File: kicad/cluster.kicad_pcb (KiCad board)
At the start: 2 copper layers, 24.5 x 36.5 mm, 16 parts, among them J1 Conn_01x07

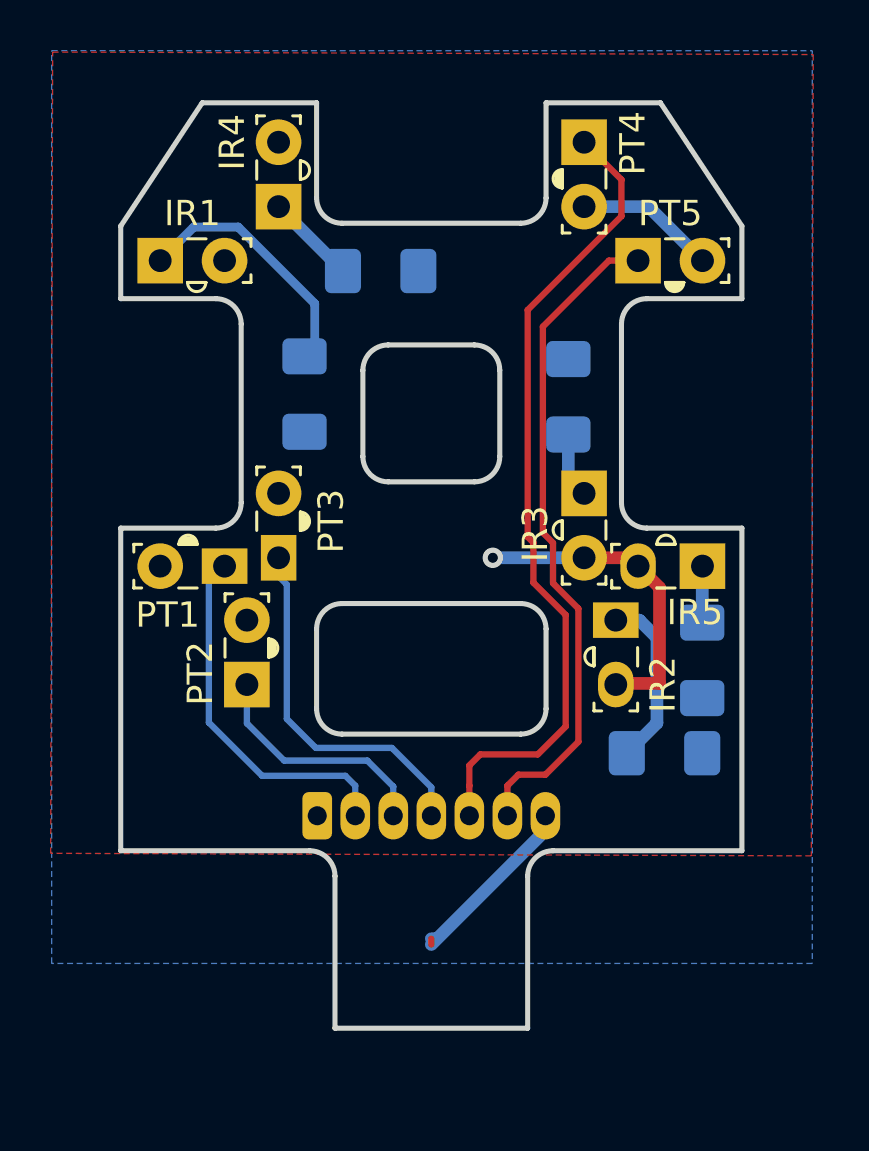
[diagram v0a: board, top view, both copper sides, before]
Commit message: Edit cluster board for choc key switch
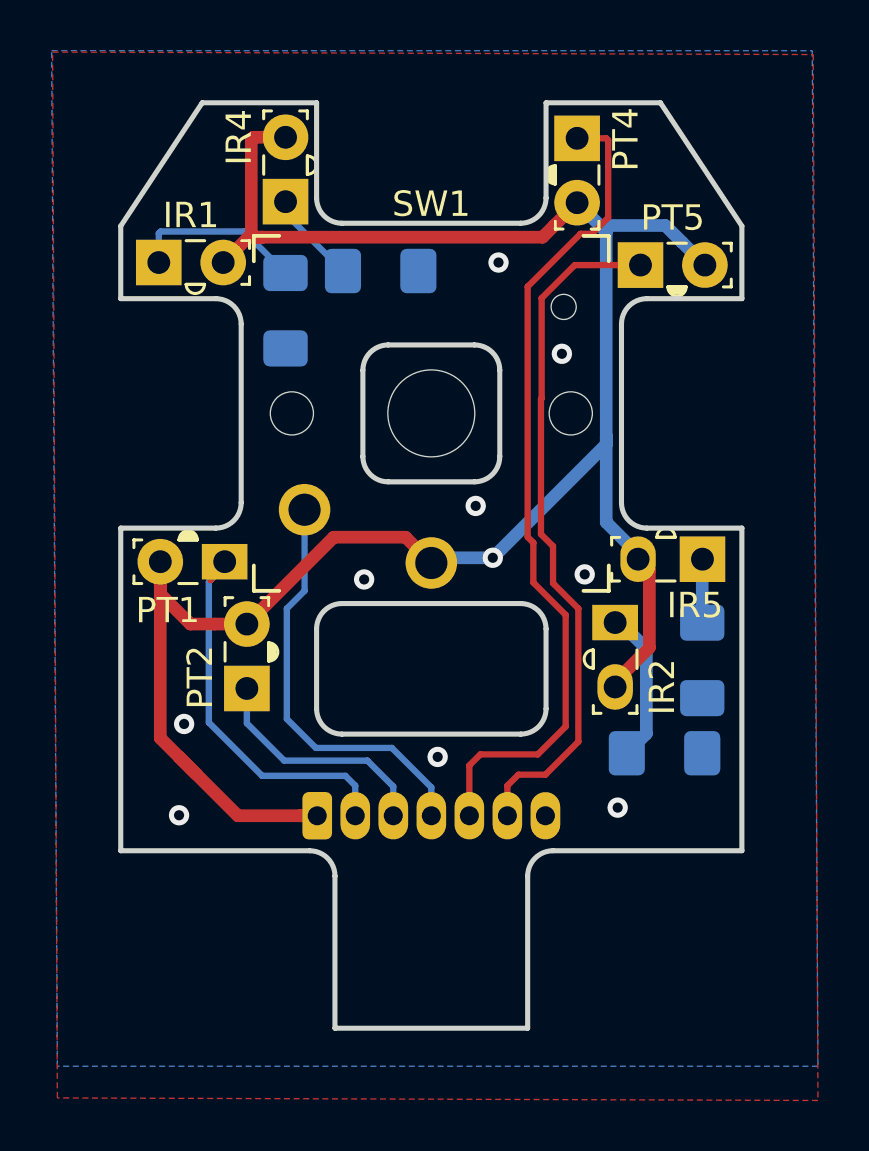
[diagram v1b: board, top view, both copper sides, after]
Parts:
- removed IR3: IR908-7C-F, lalboard:IR908-7C-F
- removed PT3: PT908-7B-F, lalboard:PT908-7C-F
- removed R3: 270, Resistor_SMD:R_1206_3216Metric_Pad1.42x1.75mm_HandSolder
- added SW1: SW_Push, lalboard:SW_CHOC, F.Cu at (162.4, 75.5)
- IR1, IR2, IR4, IR5: value IR908-7C-F -> OP140C
- PT1, PT2, PT4, PT5: value PT908-7B-F -> OP550A
- R1, R2, R4, R5: value 270 -> 150
- moved R1 3.37 mm to (156.7, 71.5)
- moved IR4 0.34 mm to (156.7, 67.2)
- moved PT4 0.32 mm to (168.2, 64.7)
- moved IR5 0.28 mm to (173.1, 81.3)
- moved PT5 0.20 mm to (170.7, 69.7)
- moved PT1 0.18 mm to (154.3, 81.4)
- moved PT2 0.16 mm to (155.2, 86.4)
- moved IR2 0.10 mm to (169.7, 83.8)
- moved IR1 0.09 mm to (151.7, 69.6)
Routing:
- net +5V: track 18.4 -> 86.6 mm
- net GND: track 7.76 -> 1.03 mm, vias 0 -> 9
- net Net-(IR1-Pad1): track 9.97 -> 6.86 mm
- net Net-(IR3-Pad1): track 2.58 -> 0.00 mm
- net C3: track 14.4 -> 16.5 mm
- net Net-(IR2-Pad1): track 6.96 -> 6.10 mm
- net C5: track 26.5 -> 27.3 mm
- net C4: track 32.2 -> 33.0 mm
- added copper zone on F.Cu, net GND
- removed copper zone on F.Cu, net +5V

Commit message: Customize
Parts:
- added R3: 5.1k, Resistor_SMD:R_0805_2012Metric_Pad1.15x1.40mm_HandSolder, B.Cu at (166.6, 80.6)
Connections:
- SW1 pad 1: +5V -> C3
- SW1 pad 2: C3 -> GND
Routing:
- net +5V: track 86.6 -> 91.3 mm, vias 1 -> 0
- net C3: track 16.5 -> 17.7 mm
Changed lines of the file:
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@@
   (general
     (thickness 1.6)
-    (drawings 172)
-    (tracks 118)
+    (drawings 174)
+    (tracks 119)
     (zones 0)
-    (modules 14)
+    (modules 15)
     (nets 12)
   )
@@
     (pad "" np_thru_hole circle (at 0 0) (size 3.429 3.429) (drill 3.429) (layers *.Cu *.Mask))
     (pad 2 thru_hole circle (at -5 3.8) (size 2.032 2.032) (drill 1.27) (layers *.Cu *.Mask)
+      (net 11 GND))
+    (pad 1 thru_hole circle (at 0 5.9) (size 2.032 2.032) (drill 1.27) (layers *.Cu *.Mask)
       (net 9 C3))
-    (pad 1 thru_hole circle (at 0 5.9) (size 2.032 2.032) (drill 1.27) (layers *.Cu *.Mask)
-      (net 1 +5V))
     (pad "" np_thru_hole circle (at 5.22 -4.2) (size 0.9906 0.9906) (drill 0.9906) (layers *.Cu *.Mask))
     (pad "" np_thru_hole circle (at 5.5 0) (size 1.7018 1.7018) (drill 1.7018) (layers *.Cu *.Mask))
     (pad "" np_thru_hole circle (at -5.5 0) (size 1.7018 1.7018) (drill 1.7018) (layers *.Cu *.Mask))
+  )
+  (module Resistor_SMD:R_0805_2012Metric_Pad1.15x1.40mm_HandSolder (layer B.Cu)
+    (at 166.6 80.575 90)
+    (descr "Resistor SMD 0805 (2012 Metric), square (rectangular) end terminal, IPC_7351 nominal with elongated pad for handsoldering. (Body size source: https://docs.google.com/spreadsheets/d/1BsfQQcO9C6DZCsRaXUlFlo91Tg2WpOkGARC1WS5S8t0/edit?usp=sharing), generated with kicad-footprint-generator")
+    (tags "resistor handsolder")
+    (attr smd)
+    (fp_text reference R3 (at 0 1.65 90) (layer B.SilkS)
+      (effects (font (size 1 1) (thickness 0.15)) (justify mirror))
+    )
+    (fp_text value 5.1k (at 0 -1.65 90) (layer B.Fab)
+      (effects (font (size 1 1) (thickness 0.15)) (justify mirror))
+    )
+    (fp_text user %R (at 0 0 90) (layer B.Fab)
+      (effects (font (size 0.5 0.5) (thickness 0.08)) (justify mirror))
+    )
+    (fp_line (start 1.85 -0.95) (end -1.85 -0.95) (layer B.CrtYd) (width 0.05))
+    (fp_line (start 1.85 0.95) (end 1.85 -0.95) (layer B.CrtYd) (width 0.05))
+    (fp_line (start -1.85 0.95) (end 1.85 0.95) (layer B.CrtYd) (width 0.05))
+    (fp_line (start -1.85 -0.95) (end -1.85 0.95) (layer B.CrtYd) (width 0.05))
+    (fp_line (start -0.261252 -0.71) (end 0.261252 -0.71) (layer B.SilkS) (width 0.12))
+    (fp_line (start -0.261252 0.71) (end 0.261252 0.71) (layer B.SilkS) (width 0.12))
+    (fp_line (start 1 -0.6) (end -1 -0.6) (layer B.Fab) (width 0.1))
+    (fp_line (start 1 0.6) (end 1 -0.6) (layer B.Fab) (width 0.1))
+    (fp_line (start -1 0.6) (end 1 0.6) (layer B.Fab) (width 0.1))
+    (fp_line (start -1 -0.6) (end -1 0.6) (layer B.Fab) (width 0.1))
+    (pad 2 smd roundrect (at 1.025 0 90) (size 1.15 1.4) (layers B.Cu B.Paste B.Mask) (roundrect_rratio 0.217391)
+      (net 1 +5V))
+    (pad 1 smd roundrect (at -1.025 0 90) (size 1.15 1.4) (layers B.Cu B.Paste B.Mask) (roundrect_rratio 0.217391)
+      (net 9 C3))
+    (model ${KISYS3DMOD}/Resistor_SMD.3dshapes/R_0805_2012Metric.wrl
+      (at (xyz 0 0 0))
+      (scale (xyz 1 1 1))
+      (rotate (xyz 0 0 0))
+    )
   )
   (module Resistor_SMD:R_1206_3216Metric_Pad1.42x1.75mm_HandSolder (layer B.Cu)
@@
       (rotate (xyz 0 0 0))
     )
+  )
+  (dimension 36.5 (width 0.15) (layer F.SilkS)
+    (gr_text "36.500 mm" (at 143.2 81.55 270) (layer F.SilkS)
+      (effects (font (size 1 1) (thickness 0.15)))
+    )
+    (feature1 (pts (xy 154.8 99.8) (xy 143.913579 99.8)))
+    (feature2 (pts (xy 154.8 63.3) (xy 143.913579 63.3)))
+    (crossbar (pts (xy 144.5 63.3) (xy 144.5 99.8)))
+    (arrow1a (pts (xy 144.5 99.8) (xy 143.913579 98.673496)))
+    (arrow1b (pts (xy 144.5 99.8) (xy 145.086421 98.673496)))
+    (arrow2a (pts (xy 144.5 63.3) (xy 143.913579 64.426504)))
+    (arrow2b (pts (xy 144.5 63.3) (xy 145.086421 64.426504)))
+  )
+  (dimension 24.5 (width 0.15) (layer F.SilkS)
+    (gr_text "24.500 mm" (at 162.45 55.4) (layer F.SilkS)
+      (effects (font (size 1 1) (thickness 0.15)))
+    )
+    (feature1 (pts (xy 174.7 68.160134) (xy 174.7 56.113579)))
+    (feature2 (pts (xy 150.2 68.160134) (xy 150.2 56.113579)))
+    (crossbar (pts (xy 150.2 56.7) (xy 174.7 56.7)))
+    (arrow1a (pts (xy 174.7 56.7) (xy 173.573496 57.286421)))
+    (arrow1b (pts (xy 174.7 56.7) (xy 173.573496 56.113579)))
+    (arrow2a (pts (xy 150.2 56.7) (xy 151.326504 57.286421)))
+    (arrow2b (pts (xy 150.2 56.7) (xy 151.326504 56.113579)))
   )
   (gr_text "finger cluster\nv0.1" (at 161.8 80.3) (layer B.SilkS)
@@
   (segment (start 169.77 86.2) (end 169.725 86.245) (width 0.5) (layer F.Cu) (net 1))
   (segment (start 170.275 81.245) (end 170.605 81.575) (width 0.5) (layer F.Cu) (net 1))
-  (via (at 164.875008 81.245) (size 0.8) (drill 0.4) (layers F.Cu B.Cu) (net 1))
-  (segment (start 162.655 81.245) (end 162.45 81.45) (width 0.5) (layer B.Cu) (net 1))
-  (segment (start 164.875008 81.245) (end 162.655 81.245) (width 0.5) (layer B.Cu) (net 1))
   (segment (start 169.349999 68.389999) (end 169.099999 68.139999) (width 0.5) (layer B.Cu) (net 1))
-  (segment (start 164.875008 81.245) (end 169.349999 76.770009) (width 0.5) (layer B.Cu) (net 1))
   (segment (start 172.340001 68.800001) (end 173.24 69.7) (width 0.5) (layer B.Cu) (net 1))
   (segment (start 171.679999 68.139999) (end 172.340001 68.800001) (width 0.5) (layer B.Cu) (net 1))
   (segment (start 169.099999 68.139999) (end 171.679999 68.139999) (width 0.5) (layer B.Cu) (net 1))
   (segment (start 168.2 67.24) (end 169.099999 68.139999) (width 0.5) (layer B.Cu) (net 1))
-  (segment (start 164.930008 81.3) (end 164.875008 81.245) (width 0.5) (layer B.Cu) (net 1))
   (segment (start 157.265 91.42) (end 157.95 91.42) (width 0.5) (layer F.Cu) (net 1))
   (segment (start 167.300001 68.139999) (end 168.2 67.24) (width 0.5) (layer F.Cu) (net 1))
@@
   (segment (start 151.76 82.672792) (end 152.947208 83.86) (width 0.5) (layer F.Cu) (net 1))
   (segment (start 151.76 81.4) (end 151.76 82.672792) (width 0.5) (layer F.Cu) (net 1))
-  (segment (start 161.434001 80.434001) (end 162.45 81.45) (width 0.5) (layer F.Cu) (net 1))
-  (segment (start 158.600999 80.434001) (end 161.434001 80.434001) (width 0.5) (layer F.Cu) (net 1))
-  (segment (start 155.175 83.86) (end 158.600999 80.434001) (width 0.5) (layer F.Cu) (net 1))
   (segment (start 170.605 81.1) (end 170.605 81.3) (width 0.5) (layer B.Cu) (net 1))
   (segment (start 169.349999 76.450001) (end 169.349999 79.844999) (width 0.5) (layer B.Cu) (net 1))
@@
   (segment (start 169.349999 76.450001) (end 169.349999 68.389999) (width 0.5) (layer B.Cu) (net 1))
   (segment (start 169.349999 76.770009) (end 169.349999 76.450001) (width 0.5) (layer B.Cu) (net 1))
+  (segment (start 168.855 79.55) (end 166.6 79.55) (width 0.5) (layer B.Cu) (net 1))
+  (segment (start 170.605 81.3) (end 168.855 79.55) (width 0.5) (layer B.Cu) (net 1))
+  (segment (start 155.139999 70.499999) (end 154.24 69.6) (width 0.5) (layer F.Cu) (net 1))
+  (segment (start 159.189685 74.549685) (end 155.139999 70.499999) (width 0.5) (layer F.Cu) (net 1))
+  (segment (start 159.189685 79.845315) (end 159.189685 74.549685) (width 0.5) (layer F.Cu) (net 1))
+  (segment (start 155.175 83.86) (end 159.189685 79.845315) (width 0.5) (layer F.Cu) (net 1))
   (segment (start 151.7 68.45) (end 151.7 69.6) (width 0.25) (layer B.Cu) (net 2))
   (segment (start 151.775001 68.374999) (end 151.7 68.45) (width 0.25) (layer B.Cu) (net 2))
@@
   (segment (start 164.384998 89) (end 166.65 89) (width 0.25) (layer F.Cu) (net 8))
   (segment (start 167.75 87.9) (end 167.75 83.5) (width 0.25) (layer F.Cu) (net 8))
-  (segment (start 157.895 88.745) (end 160.895 88.745) (width 0.25) (layer B.Cu) (net 9))
-  (segment (start 162.45 90.3) (end 162.45 91.42) (width 0.25) (layer B.Cu) (net 9))
-  (segment (start 160.895 88.745) (end 162.45 90.3) (width 0.25) (layer B.Cu) (net 9))
-  (segment (start 156.75 87.6) (end 157.895 88.745) (width 0.25) (layer B.Cu) (net 9))
-  (segment (start 156.75 87.6) (end 156.75 83.25) (width 0.25) (layer B.Cu) (net 9))
-  (segment (start 157.45 82.55) (end 157.45 79.35) (width 0.25) (layer B.Cu) (net 9))
-  (segment (start 156.75 83.25) (end 157.45 82.55) (width 0.25) (layer B.Cu) (net 9))
+  (segment (start 162.655 81.245) (end 162.45 81.45) (width 0.5) (layer B.Cu) (net 9))
+  (segment (start 166.45 81.45) (end 166.6 81.6) (width 0.25) (layer B.Cu) (net 9))
+  (segment (start 162.45 81.45) (end 166.45 81.45) (width 0.25) (layer B.Cu) (net 9))
+  (segment (start 162.45 91.07) (end 162.45 91.42) (width 0.25) (layer B.Cu) (net 9))
+  (segment (start 163.36001 90.15999) (end 162.45 91.07) (width 0.25) (layer B.Cu) (net 9))
+  (segment (start 165.04001 90.15999) (end 163.36001 90.15999) (width 0.25) (layer B.Cu) (net 9))
+  (segment (start 167.40001 87.79999) (end 165.04001 90.15999) (width 0.25) (layer B.Cu) (net 9))
+  (segment (start 167.40001 83.07501) (end 167.40001 87.79999) (width 0.25) (layer B.Cu) (net 9))
+  (segment (start 166.6 82.275) (end 167.40001 83.07501) (width 0.25) (layer B.Cu) (net 9))
+  (segment (start 166.6 81.6) (end 166.6 82.275) (width 0.25) (layer B.Cu) (net 9))
   (segment (start 165.45 90.235) (end 165.45 91.42) (width 0.25) (layer F.Cu) (net 10))
   (segment (start 165.885 89.8) (end 165.45 90.235) (width 0.25) (layer F.Cu) (net 10))
@@
   (via (at 169.8 91.1) (size 0.8) (drill 0.4) (layers F.Cu B.Cu) (net 11))
   (via (at 165.1 69.6) (size 0.8) (drill 0.4) (layers F.Cu B.Cu) (net 11))
-  (via (at 162.7 89.1) (size 0.8) (drill 0.4) (layers F.Cu B.Cu) (net 11))
   (via (at 167.6 73.2) (size 0.8) (drill 0.4) (layers F.Cu B.Cu) (net 11))
   (via (at 152.7 87.8) (size 0.8) (drill 0.4) (layers F.Cu B.Cu) (net 11))
@@
   (via (at 159.8 82.1) (size 0.8) (drill 0.4) (layers F.Cu B.Cu) (net 11))
   (via (at 168.5 81.9) (size 0.8) (drill 0.4) (layers F.Cu B.Cu) (net 11))
+  (via (at 168.3 78.1) (size 0.8) (drill 0.4) (layers F.Cu B.Cu) (net 11))
   (zone (net 11) (net_name GND) (layer B.Cu) (hatch edge 0.508)
     (connect_pads (clearance 0.508))
